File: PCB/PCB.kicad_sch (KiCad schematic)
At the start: 20 parts, among them J1 Conn_01x06_Female, U13 74HC165, U15 LT3042xMSE

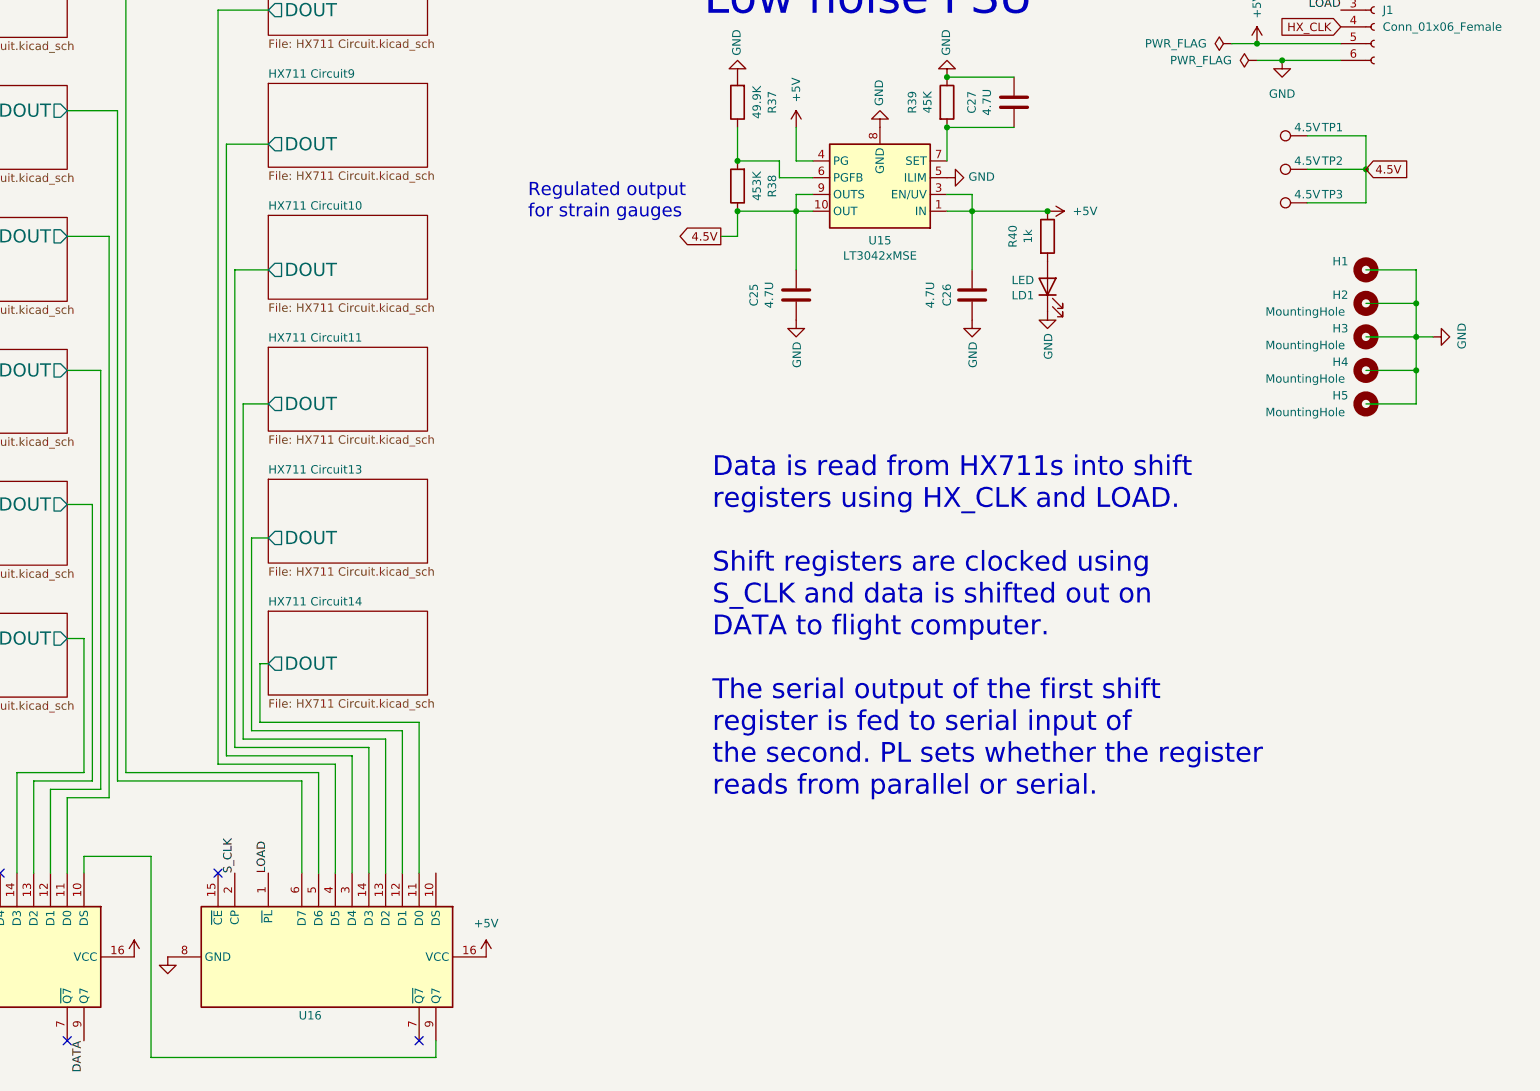
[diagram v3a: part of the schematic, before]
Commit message: Start radial layout
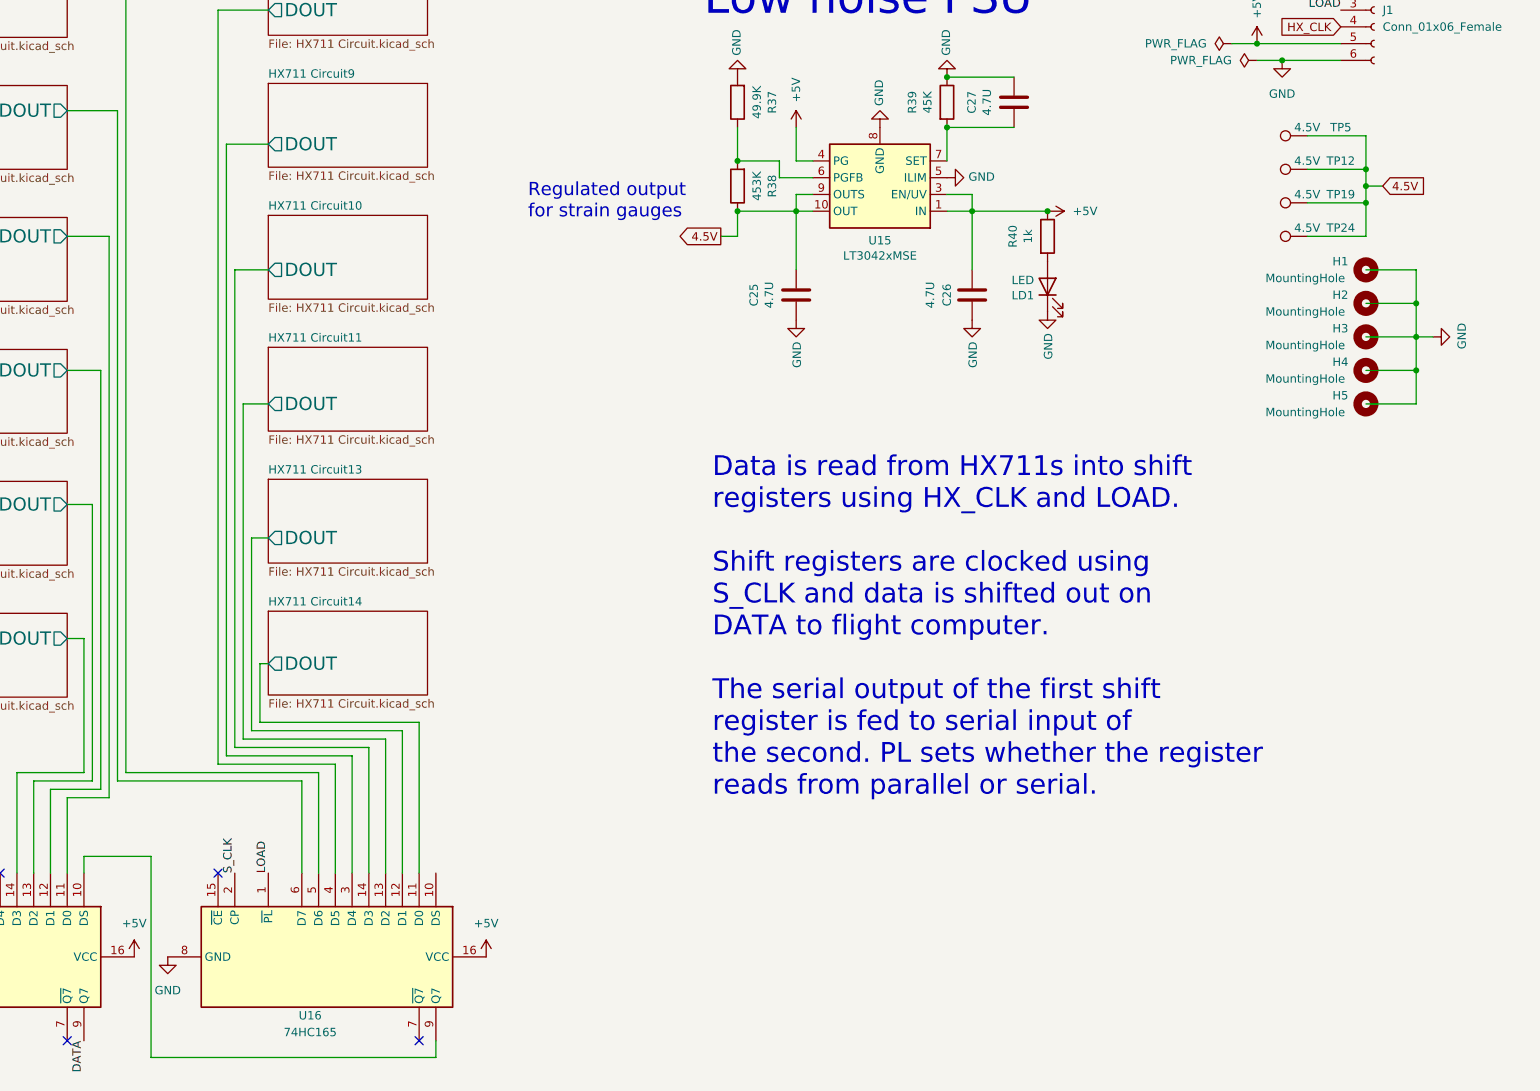
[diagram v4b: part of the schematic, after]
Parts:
- added TP12: 4.5V, Custom-footprints:Radial-Pads-With-Relief, symbol PCB-rescue:TestPoint-Connector
- H1: value (none) -> MountingHole; footprint (none) -> MountingHole:MountingHole_3.7mm_Pad_TopBottom
- H2, H3, H4: footprint (none) -> MountingHole:MountingHole_3.7mm_Pad_TopBottom
- H5: footprint (none) -> MountingHole:MountingHole_6.4mm_M6_Pad_TopBottom
- J1: footprint (none) -> Connector_JST:JST_EH_B6B-EH-A_1x06_P2.50mm_Vertical
- U16: value (none) -> 74HC165; footprint (none) -> Package_SO:SO-16_3.9x9.9mm_P1.27mm
- renumbered TP2 to TP19, TP3 to TP24, TP1 to TP5
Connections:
- net 4.5V: now also TP12.1
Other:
- moved on the sheet: TP19, TP24

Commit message: Finish radial layout
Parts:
- removed U15: LT3042xMSE, Package_SO:MSOP-10-1EP_3x3mm_P0.5mm_EP1.68x1.88mm, symbol PCB-rescue:LT3042xMSE-Regulator_Linear
- added U15: (no value), symbol Regulator_Linear:LT3042xMSE
- R38: value 453K -> (none); footprint Resistor_SMD:R_0805_2012Metric_Pad1.20x1.40mm_HandSolder -> (none)
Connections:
- net +5V: now also U15.1 (IN), U15.2 (IN), U15.3 (EN/UV), U15.4 (PG)
- net 4.5V: now also U15.10 (OUT), U15.9 (OUTS)
- net GND: now also U15.11 (GND), U15.5 (ILIM), U15.8 (GND)
- net at R37.1, R38.2: now also U15.6 (PGFB)
- net at C27.2, R39.2: now also U15.7 (SET)
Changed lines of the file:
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@@
     )
-  )
-  (symbol (lib_id "PCB-rescue:LT3042xMSE-Regulator_Linear") (at 181.61 62.23 180) (unit 1)
-    (in_bom yes) (on_board yes)
-    (property "Reference" "U15" (id 0) (at 181.61 69.215 0))
-    (property "Value" "LT3042xMSE" (id 1) (at 181.61 71.5264 0))
-    (property "Footprint" "Package_SO:MSOP-10-1EP_3x3mm_P0.5mm_EP1.68x1.88mm" (id 2) (at 181.61 70.485 0)
-      (effects (font (size 1.27 1.27)) hide)
-    )
-    (property "Datasheet" "" (id 3) (at 181.61 62.23 0)
-      (effects (font (size 1.27 1.27)) hide)
-    )
-    (pin "1")
-    (pin "10")
-    (pin "11")
-    (pin "2")
-    (pin "3")
-    (pin "4")
-    (pin "5")
-    (pin "6")
-    (pin "7")
-    (pin "8")
-    (pin "9")
   )
   (symbol (lib_id "PCB-rescue:GND-power") (at 181.61 52.07 180) (unit 1)
@@
     (in_bom yes) (on_board yes)
     (property "Reference" "R38" (id 0) (at 165.2778 60.96 90))
-    (property "Value" "453K" (id 1) (at 162.9664 60.96 90))
-    (property "Footprint" "Resistor_SMD:R_0805_2012Metric_Pad1.20x1.40mm_HandSolder" (id 2) (at 161.798 60.96 90)
+    (property "Value" "" (id 1) (at 162.9664 60.96 90))
+    (property "Footprint" "" (id 2) (at 161.798 60.96 90)
       (effects (font (size 1.27 1.27)) hide)
     )
@@
     (pin "9")
   )
+  (symbol (lib_id "Regulator_Linear:LT3042xMSE") (at 181.61 62.23 180) (unit 1)
+    (in_bom yes) (on_board yes) (fields_autoplaced)
+    (property "Reference" "U15" (id 0) (at 181.61 69.85 0))
+    (property "Value" "" (id 1) (at 181.61 72.39 0))
+    (property "Footprint" "" (id 2) (at 181.61 70.485 0)
+      (effects (font (size 1.27 1.27)) hide)
+    )
+    (property "Datasheet" "https://www.analog.com/media/en/technical-documentation/data-sheets/3042fb.pdf" (id 3) (at 181.61 62.23 0)
+      (effects (font (size 1.27 1.27)) hide)
+    )
+    (pin "1")
+    (pin "10")
+    (pin "11")
+    (pin "2")
+    (pin "3")
+    (pin "4")
+    (pin "5")
+    (pin "6")
+    (pin "7")
+    (pin "8")
+    (pin "9")
+  )
   (symbol (lib_id "PCB-rescue:+5V-power") (at 168.91 52.07 0) (unit 1)
     (in_bom yes) (on_board yes)
@@
       (reference "U13") (unit 1) (value "74HC165") (footprint "Package_SO:SO-16_3.9x9.9mm_P1.27mm")
     )
-    (path "/00000000-0000-0000-0000-0000607a5d47"
+    (path "/43ac6ffa-7b63-4fc0-b2b8-4c9c5eb4bd58"
       (reference "U15") (unit 1) (value "LT3042xMSE") (footprint "Package_SO:MSOP-10-1EP_3x3mm_P0.5mm_EP1.68x1.88mm")
     )
